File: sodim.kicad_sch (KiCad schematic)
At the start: 7 parts, among them J1 Edge_Conn_Bus_DDR5_SODIMM_1xD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, U7 AT24CS01_SOT23

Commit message: Loclib
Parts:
- C7: footprint antmicro-footprints:C_0402_1005Metric -> lpddr5-testbed-footprints:C_0402_1005Metric; symbol antmicroCapacitors0402:C_4u7_0402 -> lpddr5-testbed:C_4u7_0402
- J1: footprint antmicro-footprints:Edge_Conn_Bus_DDR5_SODIMM -> lpddr5-testbed-footprints:Edge_Conn_Bus_DDR5_SODIMM; symbol antmicroMemoryConnectorsPCCardSockets:Edge_Conn_Bus_DDR5_SODIMM_1xDetectPin -> lpddr5-testbed:Edge_Conn_Bus_DDR5_SODIMM_1xDetectPin
- R26, R27: footprint antmicro-footprints:R_0402_1005Metric -> lpddr5-testbed-footprints:R_0402_1005Metric; symbol antmicroResistors0402:R_0R_0402 -> lpddr5-testbed:R_0R_0402
- R28: footprint antmicro-footprints:R_0402_1005Metric -> lpddr5-testbed-footprints:R_0402_1005Metric; symbol antmicroResistors0402:R_200k_0402 -> lpddr5-testbed:R_200k_0402
- R99: footprint antmicro-footprints:R_0402_1005Metric -> lpddr5-testbed-footprints:R_0402_1005Metric; symbol antmicroResistors0402:R_100k_0402 -> lpddr5-testbed:R_100k_0402
- U7: footprint antmicro-footprints:SOT-23-5 -> lpddr5-testbed-footprints:SOT-23-5; symbol antmicroMemory:AT24CS01_SOT23 -> lpddr5-testbed:AT24CS01_SOT23
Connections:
- net HSCL: now also J1.7 (PWR_GOOD); no longer J1.4 (HSCL)
- net HSDA: now also J1.108 (ALERT_n); no longer J1.6 (HSDA)
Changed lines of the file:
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@@
     (effects (font (size 1.27 1.27)) (justify left))
   )
-  (symbol (lib_name "Edge_Conn_Bus_DDR5_SODIMM_1xDetectPin_1") (lib_id "antmicroMemoryConnectorsPCCardSockets:Edge_Conn_Bus_DDR5_SODIMM_1xDetectPin") (at 170.18 30.48 0) (unit 1)
+  (symbol (lib_id "lpddr5-testbed:Edge_Conn_Bus_DDR5_SODIMM_1xDetectPin") (at 170.18 30.48 0) (unit 1)
     (in_bom yes) (on_board yes)
     (property "Reference" "J1" (id 0) (at 182.88 26.67 0))
     (property "Value" "Edge_Conn_Bus_DDR5_SODIMM_1xDetectPin" (id 1) (at 185.42 54.61 0))
-    (property "Footprint" "antmicro-footprints:Edge_Conn_Bus_DDR5_SODIMM" (id 2) (at 222.25 43.18 0)
+    (property "Footprint" "lpddr5-testbed-footprints:Edge_Conn_Bus_DDR5_SODIMM" (id 2) (at 222.25 43.18 0)
       (effects (font (size 1.27 1.27)) (justify left bottom) hide)
     )
@@
     (pin "260")
   )
-  (symbol (lib_id "antmicroResistors0402:R_0R_0402") (at 216.535 50.8 0) (mirror x) (unit 1)
+  (symbol (lib_id "lpddr5-testbed:R_0R_0402") (at 216.535 50.8 0) (mirror x) (unit 1)
     (in_bom yes) (on_board yes)
     (property "Reference" "R27" (id 0) (at 216.535 49.53 0)
@@
       (effects (font (size 1.27 1.27) (thickness 0.15)) (justify left bottom) hide)
     )
-    (property "Footprint" "antmicro-footprints:R_0402_1005Metric" (id 2) (at 236.855 35.56 0)
+    (property "Footprint" "lpddr5-testbed-footprints:R_0402_1005Metric" (id 2) (at 236.855 35.56 0)
       (effects (font (size 1.27 1.27) (thickness 0.15)) (justify left bottom) hide)
     )
@@
     (pin "1")
   )
-  (symbol (lib_id "antmicroResistors0402:R_0R_0402") (at 216.535 48.26 0) (mirror x) (unit 1)
+  (symbol (lib_id "lpddr5-testbed:R_0R_0402") (at 216.535 48.26 0) (mirror x) (unit 1)
     (in_bom yes) (on_board yes)
     (property "Reference" "R26" (id 0) (at 216.535 46.99 0)
@@
       (effects (font (size 1.27 1.27) (thickness 0.15)) (justify left bottom) hide)
     )
-    (property "Footprint" "antmicro-footprints:R_0402_1005Metric" (id 2) (at 236.855 33.02 0)
+    (property "Footprint" "lpddr5-testbed-footprints:R_0402_1005Metric" (id 2) (at 236.855 33.02 0)
       (effects (font (size 1.27 1.27) (thickness 0.15)) (justify left bottom) hide)
     )
@@
     (pin "2")
   )
-  (symbol (lib_id "antmicropower:+5V") (at 161.29 25.4 0) (unit 1)
+  (symbol (lib_id "lpddr5-testbed:+5V") (at 161.29 25.4 0) (unit 1)
     (in_bom yes) (on_board yes)
     (property "Reference" "#PWR0142" (id 0) (at 176.53 27.94 0)
@@
     (pin "1")
   )
-  (symbol (lib_id "antmicropower:+1V8") (at 245.11 66.04 0) (unit 1)
+  (symbol (lib_id "lpddr5-testbed:+1V8") (at 245.11 66.04 0) (unit 1)
     (in_bom yes) (on_board yes) (fields_autoplaced)
     (property "Reference" "#PWR0140" (id 0) (at 260.35 68.58 0)
@@
     (pin "1")
   )
-  (symbol (lib_id "antmicroResistors0402:R_200k_0402") (at 161.29 34.29 270) (unit 1)
+  (symbol (lib_id "lpddr5-testbed:R_200k_0402") (at 161.29 34.29 270) (unit 1)
     (in_bom yes) (on_board yes)
     (property "Reference" "R28" (id 0) (at 162.56 35.56 90)
@@
       (effects (font (size 1.27 1.27) (thickness 0.15)) (justify left bottom) hide)
     )
-    (property "Footprint" "antmicro-footprints:R_0402_1005Metric" (id 2) (at 146.05 54.61 0)
+    (property "Footprint" "lpddr5-testbed-footprints:R_0402_1005Metric" (id 2) (at 146.05 54.61 0)
       (effects (font (size 1.27 1.27) (thickness 0.15)) (justify left bottom) hide)
     )
@@
     (pin "2")
   )
-  (symbol (lib_id "antmicroCapacitors0402:C_4u7_0402") (at 245.11 72.39 90) (unit 1)
+  (symbol (lib_id "lpddr5-testbed:C_4u7_0402") (at 245.11 72.39 90) (unit 1)
     (in_bom yes) (on_board yes)
     (property "Reference" "C7" (id 0) (at 245.745 67.945 90)
@@
       (effects (font (size 1.27 1.27) (thickness 0.15)) (justify left bottom) hide)
     )
-    (property "Footprint" "antmicro-footprints:C_0402_1005Metric" (id 2) (at 257.81 52.07 0)
+    (property "Footprint" "lpddr5-testbed-footprints:C_0402_1005Metric" (id 2) (at 257.81 52.07 0)
       (effects (font (size 1.27 1.27) (thickness 0.15)) (justify left bottom) hide)
     )
@@
     (pin "1")
   )
-  (symbol (lib_id "antmicropower:PWR_FLAG") (at 167.64 29.21 0) (unit 1)
+  (symbol (lib_id "lpddr5-testbed:PWR_FLAG") (at 167.64 29.21 0) (unit 1)
     (in_bom yes) (on_board yes)
     (property "Reference" "#FLG01" (id 0) (at 167.64 27.305 0)
@@
     (pin "1")
   )
-  (symbol (lib_id "antmicroResistors0402:R_100k_0402") (at 161.29 41.91 270) (unit 1)
+  (symbol (lib_id "lpddr5-testbed:R_100k_0402") (at 161.29 41.91 270) (unit 1)
     (in_bom yes) (on_board yes)
     (property "Reference" "R99" (id 0) (at 162.56 43.18 90)
@@
       (effects (font (size 1.27 1.27) (thickness 0.15)) (justify left bottom) hide)
     )
-    (property "Footprint" "antmicro-footprints:R_0402_1005Metric" (id 2) (at 146.05 62.23 0)
+    (property "Footprint" "lpddr5-testbed-footprints:R_0402_1005Metric" (id 2) (at 146.05 62.23 0)
       (effects (font (size 1.27 1.27) (thickness 0.15)) (justify left bottom) hide)
     )
@@
     (pin "2")
   )
-  (symbol (lib_id "antmicroMemoryConnectorsPCCardSockets:Edge_Conn_Bus_DDR5_SODIMM_1xDetectPin") (at 85.09 104.14 0) (unit 2)
+  (symbol (lib_id "lpddr5-testbed:Edge_Conn_Bus_DDR5_SODIMM_1xDetectPin") (at 85.09 104.14 0) (unit 2)
     (in_bom yes) (on_board yes)
     (property "Reference" "J1" (id 0) (at 102.87 93.98 0))
     (property "Value" "Edge_Conn_Bus_DDR5_SODIMM_1xDetectPin" (id 1) (at 102.87 97.79 0))
-    (property "Footprint" "antmicro-footprints:Edge_Conn_Bus_DDR5_SODIMM" (id 2) (at 137.16 116.84 0)
+    (property "Footprint" "lpddr5-testbed-footprints:Edge_Conn_Bus_DDR5_SODIMM" (id 2) (at 137.16 116.84 0)
       (effects (font (size 1.27 1.27)) (justify left bottom) hide)
     )
@@
     (pin "260")
   )
-  (symbol (lib_id "antmicroMemoryConnectorsPCCardSockets:Edge_Conn_Bus_DDR5_SODIMM_1xDetectPin") (at 237.49 104.14 0) (unit 3)
+  (symbol (lib_id "lpddr5-testbed:Edge_Conn_Bus_DDR5_SODIMM_1xDetectPin") (at 237.49 104.14 0) (unit 3)
     (in_bom yes) (on_board yes)
     (property "Reference" "J1" (id 0) (at 255.27 96.52 0))
     (property "Value" "Edge_Conn_Bus_DDR5_SODIMM_1xDetectPin" (id 1) (at 255.27 99.06 0))
-    (property "Footprint" "antmicro-footprints:Edge_Conn_Bus_DDR5_SODIMM" (id 2) (at 289.56 116.84 0)
+    (property "Footprint" "lpddr5-testbed-footprints:Edge_Conn_Bus_DDR5_SODIMM" (id 2) (at 289.56 116.84 0)
       (effects (font (size 1.27 1.27)) (justify left bottom) hide)
     )
@@
     (pin "260")
   )
-  (symbol (lib_id "antmicroMemory:AT24CS01_SOT23") (at 219.71 68.58 0) (unit 1)
+  (symbol (lib_id "lpddr5-testbed:AT24CS01_SOT23") (at 219.71 68.58 0) (unit 1)
     (in_bom yes) (on_board yes) (fields_autoplaced)
     (property "Reference" "U7" (id 0) (at 229.87 60.96 0)
@@
       (effects (font (size 1.27 1.27) (thickness 0.15)))
     )
-    (property "Footprint" "antmicro-footprints:SOT-23-5" (id 2) (at 255.27 76.2 0)
-      (effects (font (size 1.27 1.27) (thickness 0.15)) (justify left bottom) hide)
-    )
+    (property "Footprint" "lpddr5-testbed-footprints:SOT-23-5" (id 2) (at 255.27 76.2 0)
+      (effects (font (size 1.27 1.27) (thickness 0.15)) (justify left bottom) hide)
+    )

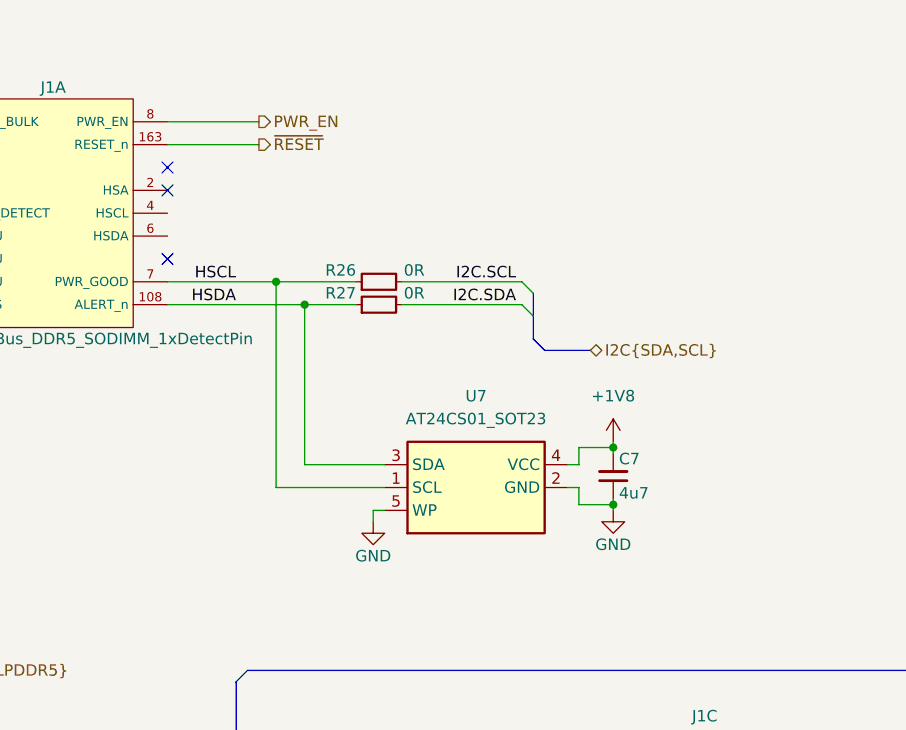
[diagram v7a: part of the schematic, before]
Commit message: [#52974] pcb: finish routing, DRC clean
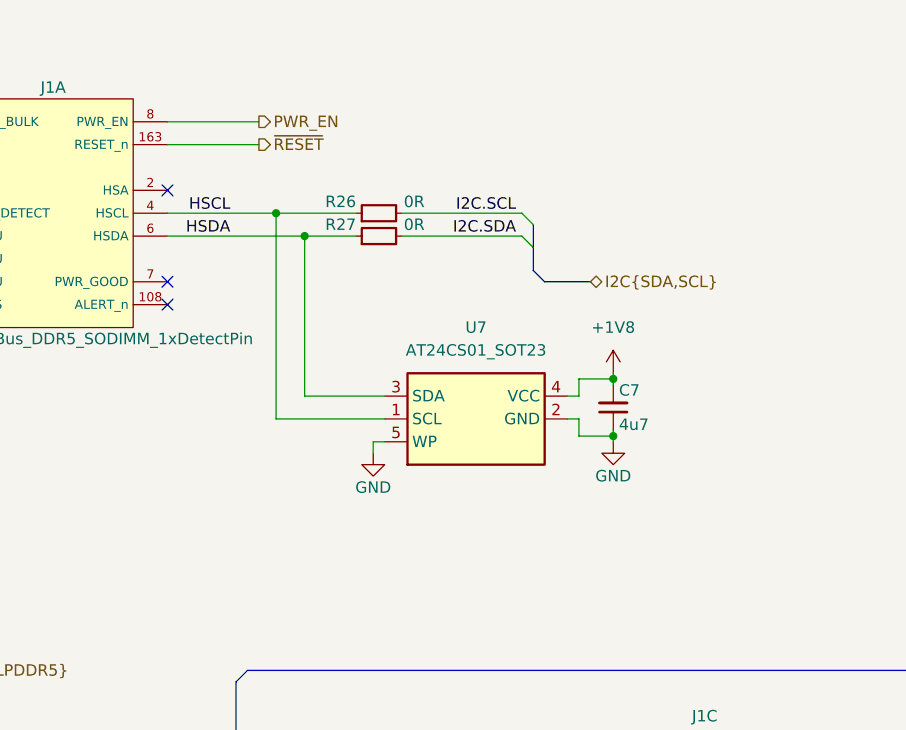
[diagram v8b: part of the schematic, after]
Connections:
- net HSCL: now also J1.4 (HSCL); no longer J1.7 (PWR_GOOD)
- net HSDA: now also J1.6 (HSDA); no longer J1.108 (ALERT_n)
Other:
- moved on the sheet: C7, R26, R27, U7
